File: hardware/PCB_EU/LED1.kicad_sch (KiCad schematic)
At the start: 29 parts, among them J501 LED1 + / GND, Q501 IRF540ZPBF, U501 LM3429MH/NOPB

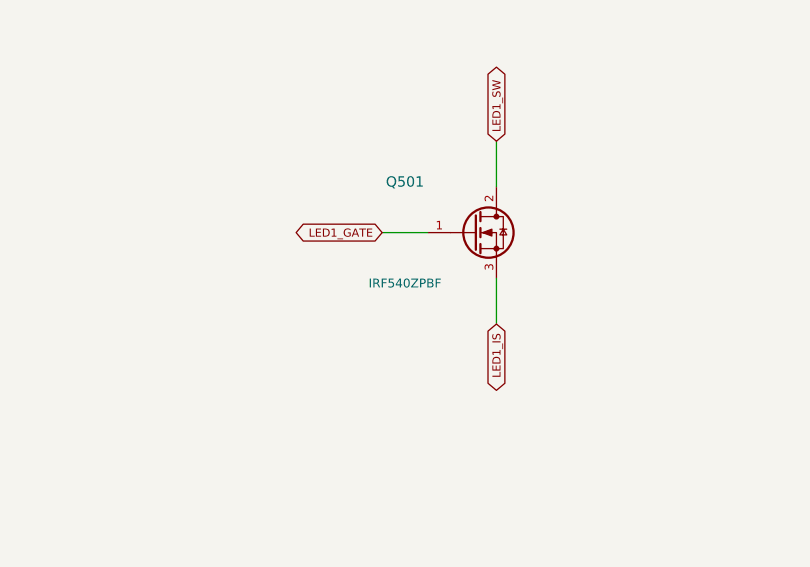
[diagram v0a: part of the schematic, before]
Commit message: PCB_EU: hand-route LED2 power loop, 5 mm cap footprint, TK22E10N1 switches
- C508-C510, C608, C609 (EEUFR1J101LB) use CP_Radial_D8.0mm_P5.00mm, the
  real 5 mm lead pitch; the 3.5 mm footprint is removed and the 3D fit check
  has no known issues left.
- LED2 is placed and routed like LED1: R601 under Q601, D601 anodes toward
  the switch, C611 between C609 leads, wide SW/IS/OUT/GND copper, LED+ and
  the gate on In2. Eight new connected groups are checked.
- route_board.py drops session copper of nets the plan now routes
  (replace_session_nets) and session vias that break hole spacing, and no
  longer prunes GND stitching vias before the pours exist.
- Q501/Q601: IRF540Z -> Toshiba TK22E10N1 (28 nC instead of 42 nC gate
  charge for the 7 V LM3429 driver); BOM 78.59 -> 77.95 EUR.

0 unrouted, DRC 0, schematic parity 0; rebuild is byte-identical.

Co-Authored-By: Claude Opus 5.5 (1M context) <noreply@anthropic.com>
Claude-Session: https://claude.ai/code/session_01AxccZX6Cb4FnRKJMrFYMSX
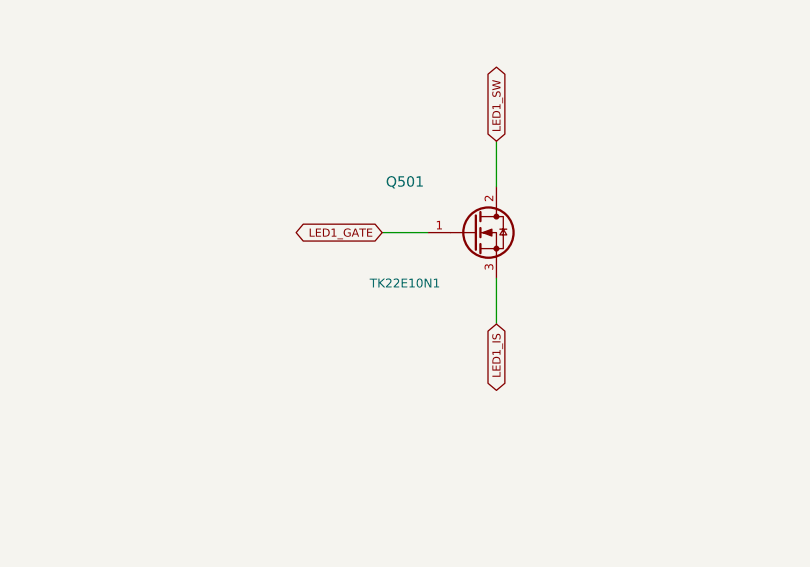
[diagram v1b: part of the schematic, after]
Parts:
- C508, C509, C510: footprint Capacitor_THT:CP_Radial_D8.0mm_P3.50mm -> Capacitor_THT:CP_Radial_D8.0mm_P5.00mm
- Q501: value IRF540ZPBF -> TK22E10N1; MPN IRF540ZPBF -> TK22E10N1
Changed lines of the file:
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@@
 (symbol (lib_id "EU:NMOS") (at 299.72 59.69 0) (unit 1) (in_bom yes) (on_board yes) (dnp no)
 (property "Reference" "Q501" (at 292.1 54.05 0) (effects (font (size 1.15 1.15)) ))
-(property "Value" "IRF540ZPBF" (at 292.1 65.33 0) (effects (font (size 0.98 0.98)) ))
+(property "Value" "TK22E10N1" (at 292.1 65.33 0) (effects (font (size 0.98 0.98)) ))
 (property "Footprint" "Package_TO_SOT_THT:TO-220-3_Vertical" (at 299.72 59.69 0) (effects (font (size 1 1)) (hide yes)))
-(property "Datasheet" "" (at 299.72 59.69 0) (effects (font (size 1 1)) (hide yes)))
-(property "MPN" "IRF540ZPBF" (at 299.72 59.69 0) (effects (font (size 1 1)) (hide yes)))
+(property "Datasheet" "https://docs.rs-online.com/8d7e/0900766b81294f79.pdf" (at 299.72 59.69 0) (effects (font (size 1 1)) (hide yes)))
+(property "MPN" "TK22E10N1" (at 299.72 59.69 0) (effects (font (size 1 1)) (hide yes)))
 (property "Design_note" "Drain tab live. Separate insulated heatsink; exact assembly placement pending" (at 299.72 59.69 0) (effects (font (size 1 1)) (hide yes)))
 (property "FootprintStatus" "PACKAGE ONLY - verify before PCB" (at 299.72 59.69 0) (effects (font (size 1 1)) (hide yes)))
@@
 (property "Reference" "C508" (at 241.3 174.7 0) (effects (font (size 1.15 1.15)) ))
 (property "Value" "100u 63V" (at 241.3 185.98 0) (effects (font (size 0.98 0.98)) ))
-(property "Footprint" "Capacitor_THT:CP_Radial_D8.0mm_P3.50mm" (at 241.3 180.34 0) (effects (font (size 1 1)) (hide yes)))
+(property "Footprint" "Capacitor_THT:CP_Radial_D8.0mm_P5.00mm" (at 241.3 180.34 0) (effects (font (size 1 1)) (hide yes)))
 (property "Datasheet" "" (at 241.3 180.34 0) (effects (font (size 1 1)) (hide yes)))
 (property "MPN" "EEUFR1J101LB" (at 241.3 180.34 0) (effects (font (size 1 1)) (hide yes)))
@@
 (property "Reference" "C509" (at 308.61 174.7 0) (effects (font (size 1.15 1.15)) ))
 (property "Value" "100u 63V" (at 308.61 185.98 0) (effects (font (size 0.98 0.98)) ))
-(property "Footprint" "Capacitor_THT:CP_Radial_D8.0mm_P3.50mm" (at 308.61 180.34 0) (effects (font (size 1 1)) (hide yes)))
+(property "Footprint" "Capacitor_THT:CP_Radial_D8.0mm_P5.00mm" (at 308.61 180.34 0) (effects (font (size 1 1)) (hide yes)))
 (property "Datasheet" "" (at 308.61 180.34 0) (effects (font (size 1 1)) (hide yes)))
 (property "MPN" "EEUFR1J101LB" (at 308.61 180.34 0) (effects (font (size 1 1)) (hide yes)))
@@
 (property "Reference" "C510" (at 374.65 174.7 0) (effects (font (size 1.15 1.15)) ))
 (property "Value" "100u 63V" (at 374.65 185.98 0) (effects (font (size 0.98 0.98)) ))
-(property "Footprint" "Capacitor_THT:CP_Radial_D8.0mm_P3.50mm" (at 374.65 180.34 0) (effects (font (size 1 1)) (hide yes)))
+(property "Footprint" "Capacitor_THT:CP_Radial_D8.0mm_P5.00mm" (at 374.65 180.34 0) (effects (font (size 1 1)) (hide yes)))
 (property "Datasheet" "" (at 374.65 180.34 0) (effects (font (size 1 1)) (hide yes)))
 (property "MPN" "EEUFR1J101LB" (at 374.65 180.34 0) (effects (font (size 1 1)) (hide yes)))
